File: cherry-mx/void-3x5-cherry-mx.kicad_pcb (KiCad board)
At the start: 2 copper layers, 140.5 x 112.5 mm, 81 parts, among them J1 Conn_01x02, J2 Conn_01x03_MountingPin, J3 Conn_01x02

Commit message: added hybrid
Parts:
- J2: moved to F.Cu
- moved D14 0.36 mm to (169.2, 78.2)
- moved S12 0.36 mm to (156.1, 58.1)
- moved L2 0.36 mm to (94.8, 84.3)
- moved D16 0.36 mm to (156.0, 118.7)
- moved D9 0.36 mm to (129.1, 47.1)
- moved J2 0.36 mm to (212.2, 103.2), turned to 0 degrees
- moved SW_SPDT1 0.36 mm to (216.7, 93.7)
- moved R3 0.36 mm to (209.2, 89.2)
- moved D12 0.36 mm to (149.1, 55.6)
- moved L11 0.36 mm to (156.1, 73.1)
- moved S10 0.36 mm to (156.1, 98.2)
- moved D2 0.36 mm to (88.1, 87.6)
- moved L21 0.36 mm to (94.2, 79.4)
- moved S3 0.36 mm to (93.2, 69.4)
- moved S5 0.36 mm to (116.0, 74.7)
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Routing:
- net VCC: track 618.6 -> 626.4 mm
- net col_middle: track 205.6 -> 207.3 mm
- net col_pinky: track 227.1 -> 227.8 mm
- net Net-(L16-DOUT): track 44.6 -> 45.1 mm
- net row_thumb: track 160.7 -> 160.2 mm
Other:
- outline, holes or cut-outs redrawn

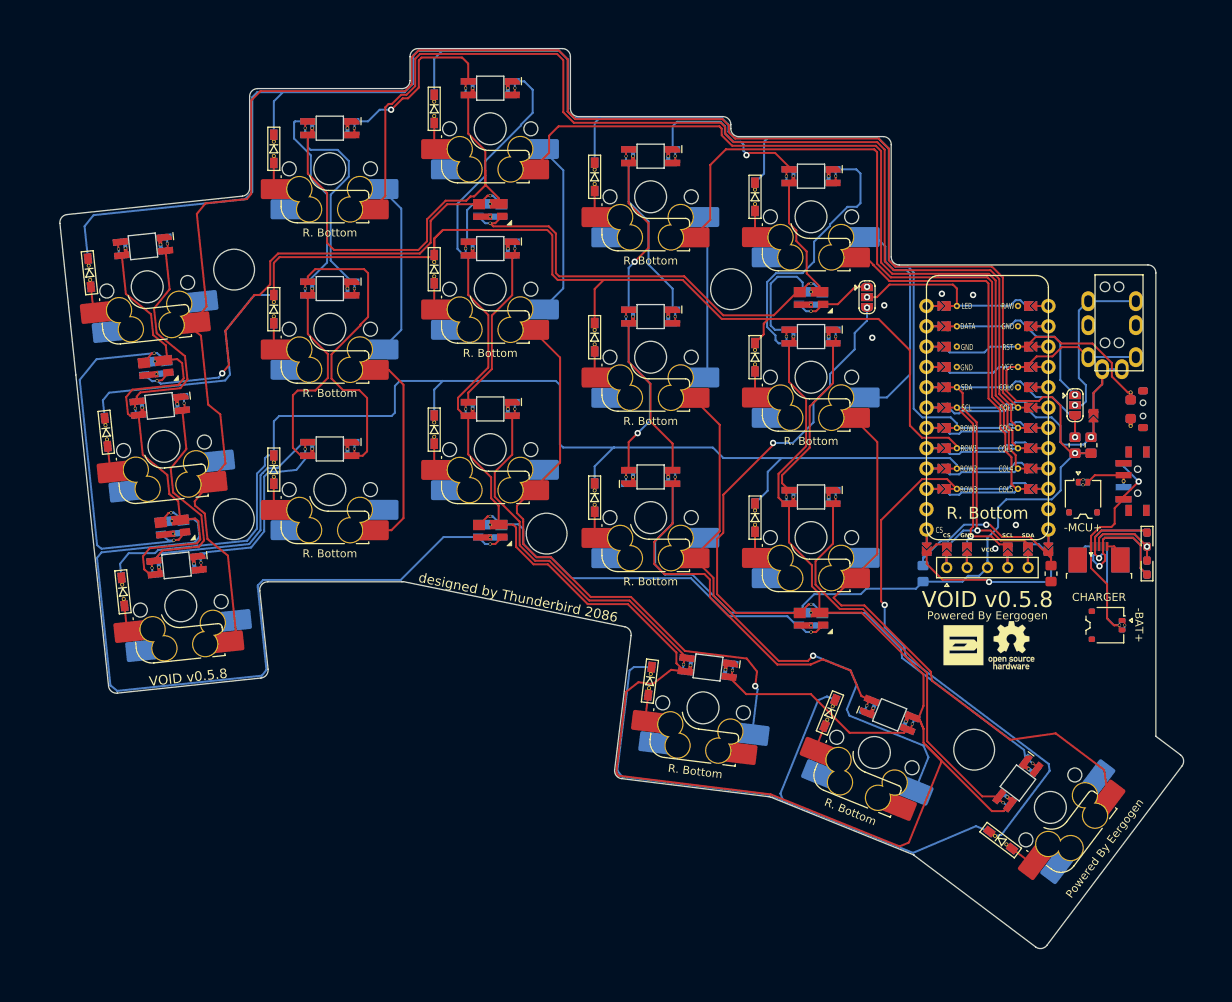
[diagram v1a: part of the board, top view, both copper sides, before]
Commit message: added choc
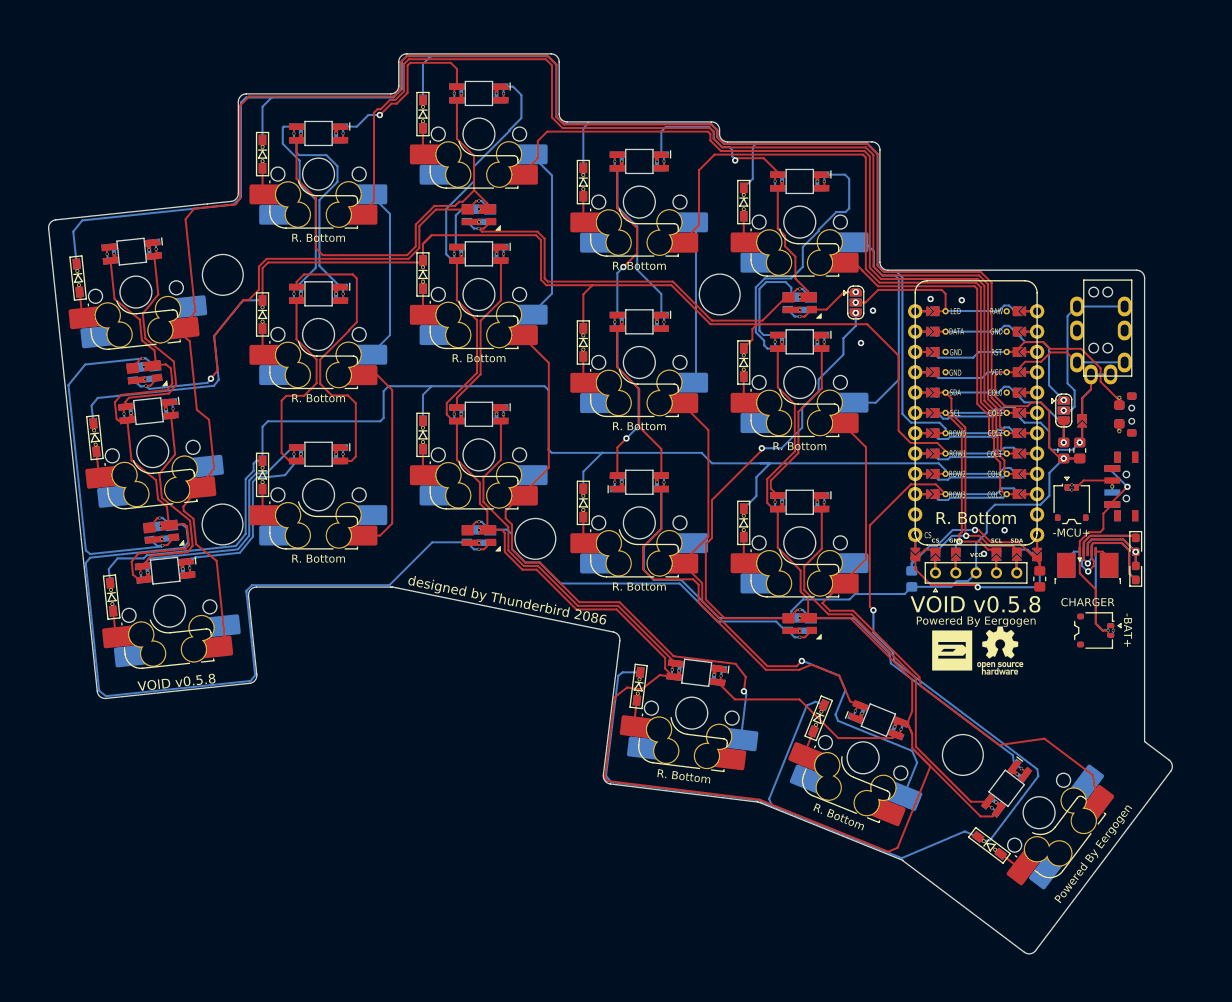
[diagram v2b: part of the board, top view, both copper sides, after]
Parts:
- moved D6 1.56 mm to (107.6, 52.8)
- moved JP1 1.56 mm to (181.8, 71.4)
- moved L12 1.56 mm to (154.7, 53.7)
- moved LED2 1.56 mm to (216.8, 101.7)
- moved LED4 1.56 mm to (216.8, 101.7)
- moved S4 1.56 mm to (114.6, 95.4)
- moved D16 1.56 mm to (154.6, 119.4)
- moved LOGO2 1.56 mm to (199.8, 114.9)
- moved L17 1.56 mm to (184.6, 123.6)
- moved D5 1.56 mm to (107.6, 72.9)
- moved S2 1.56 mm to (93.9, 90.0)
- moved L8 1.56 mm to (134.7, 65.3)
- moved L9 1.56 mm to (134.7, 45.2)
- moved L11 1.56 mm to (154.7, 73.8)
- moved L19 1.56 mm to (174.8, 71.4)
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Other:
- outline, holes or cut-outs redrawn

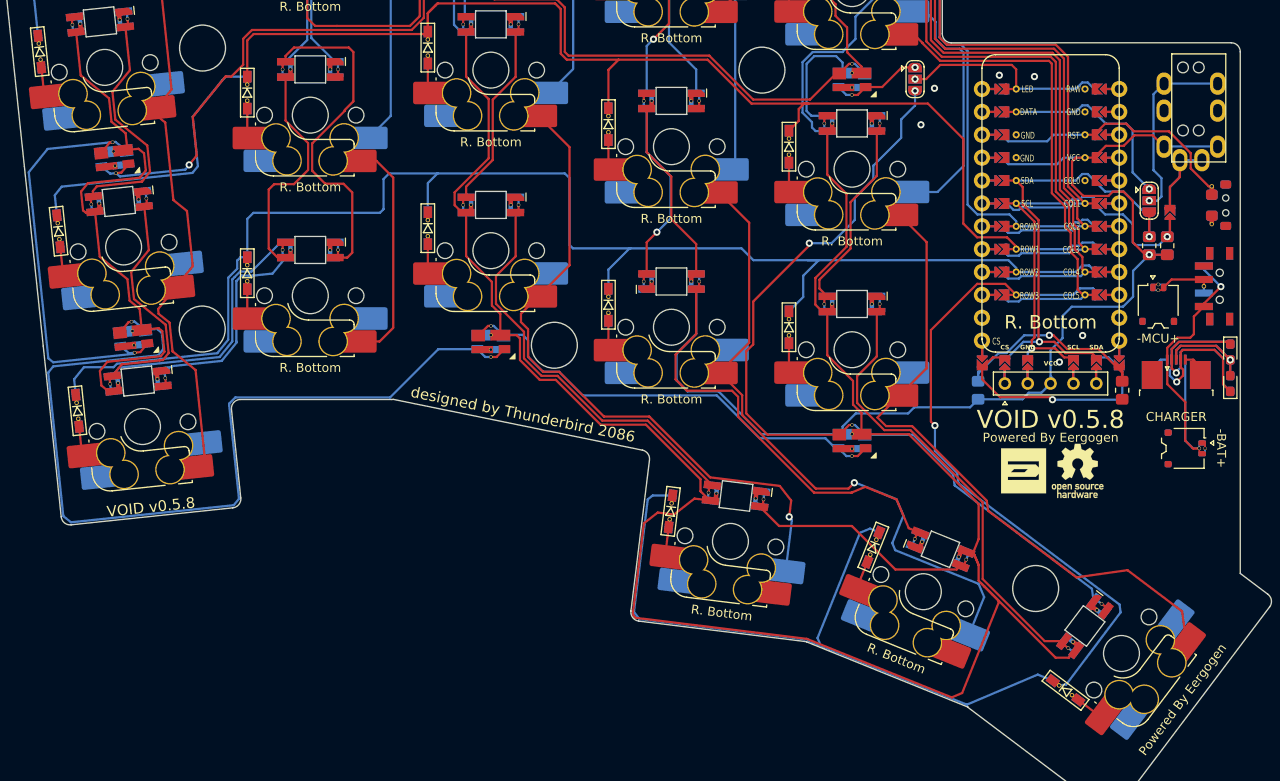
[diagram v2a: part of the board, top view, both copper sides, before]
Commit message: added holes for oled window
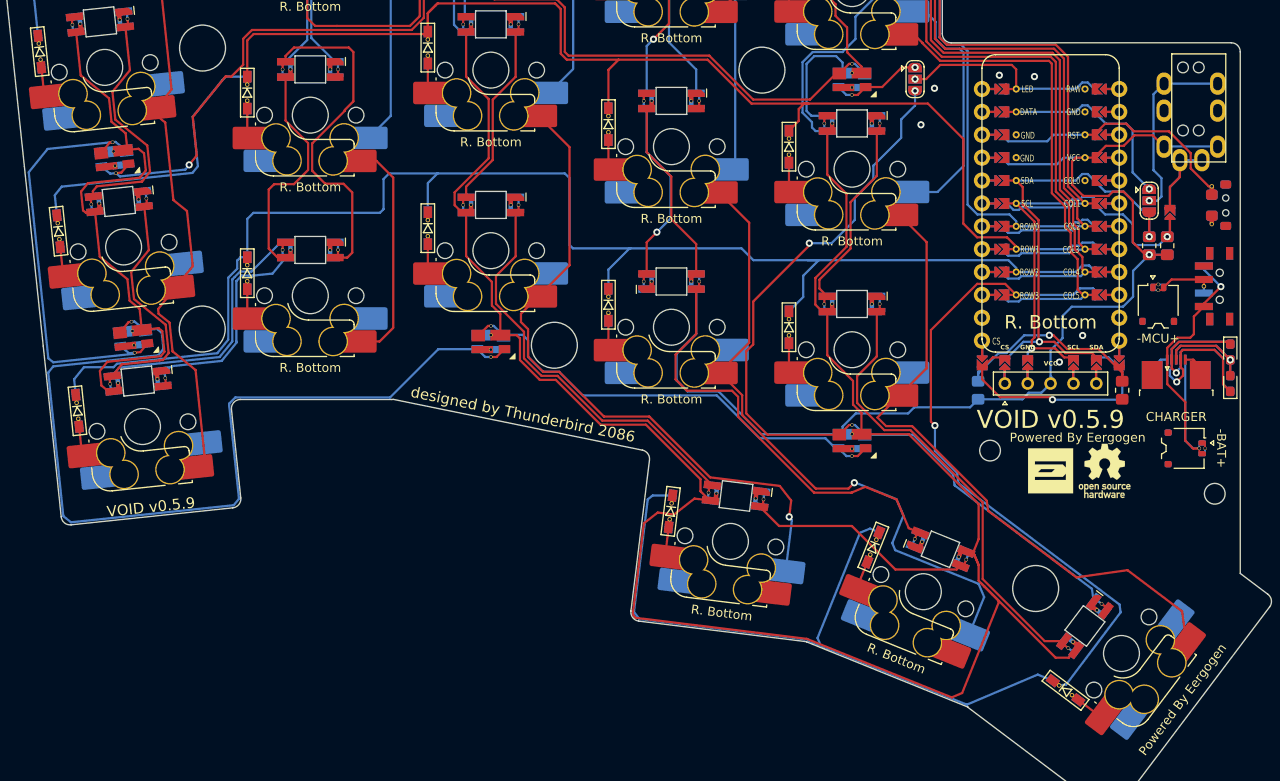
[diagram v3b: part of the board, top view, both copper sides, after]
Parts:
- moved LOGO1 3.00 mm to (196.8, 114.9)
- moved LOGO2 3.00 mm to (202.8, 114.9)
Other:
- outline, holes or cut-outs redrawn
- board text added: "VOID v0.5.9"
- board text removed: "VOID v0.5.8"

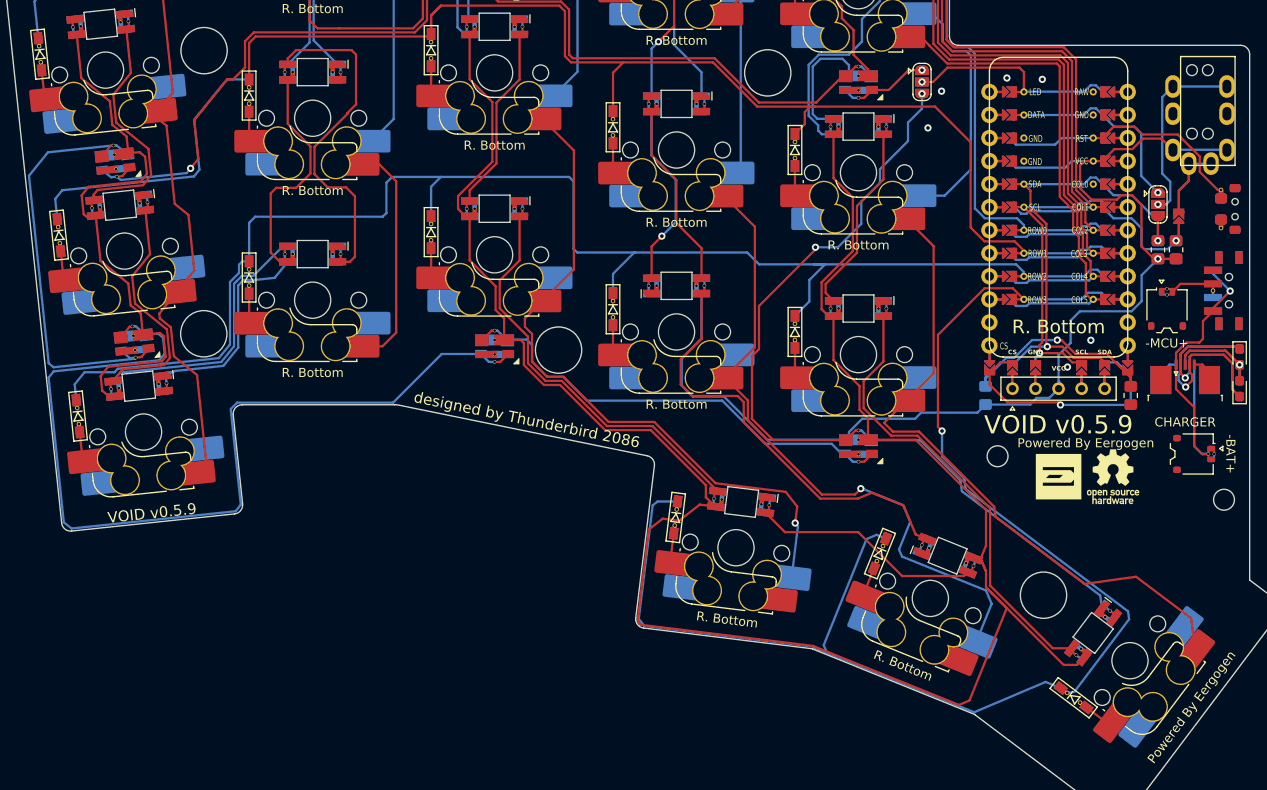
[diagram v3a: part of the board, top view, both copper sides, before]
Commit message: usb-c mod for hybrid
* updated
  - submodule
  - ergogen yaml
  - schematic and pcb
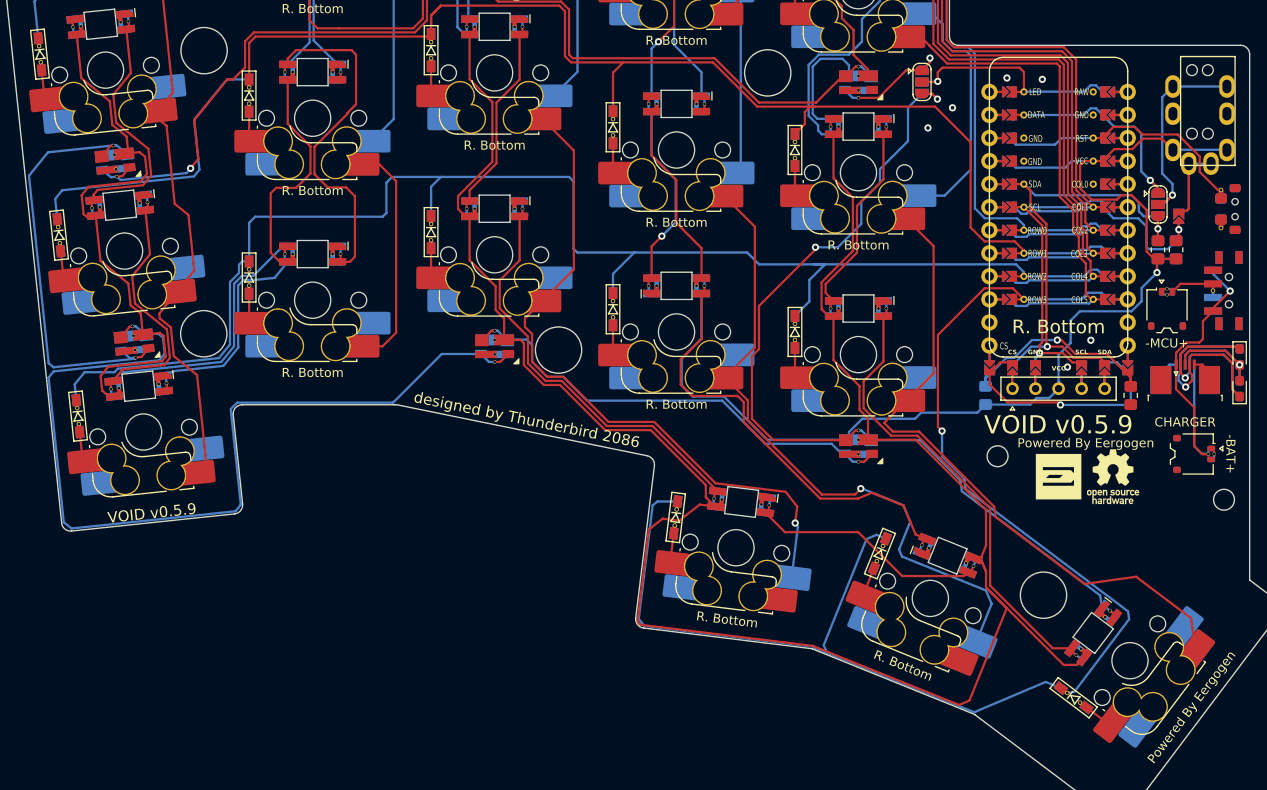
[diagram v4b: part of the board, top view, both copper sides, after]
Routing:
- net LED_PER_KEY: track 93.4 -> 97.3 mm
- net LED_UNDERGLOW: track 10.1 -> 13.5 mm
- net LED: track 24.5 -> 26.9 mm
- net Net-(JP2-C): track 20.9 -> 22.9 mm
- net DATA: track 22.7 -> 24.4 mm
- net VCC: track 626.4 -> 627.6 mm
- net Net-(JP3-B): track 13.8 -> 14.8 mm
